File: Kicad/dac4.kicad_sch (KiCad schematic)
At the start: 10 parts

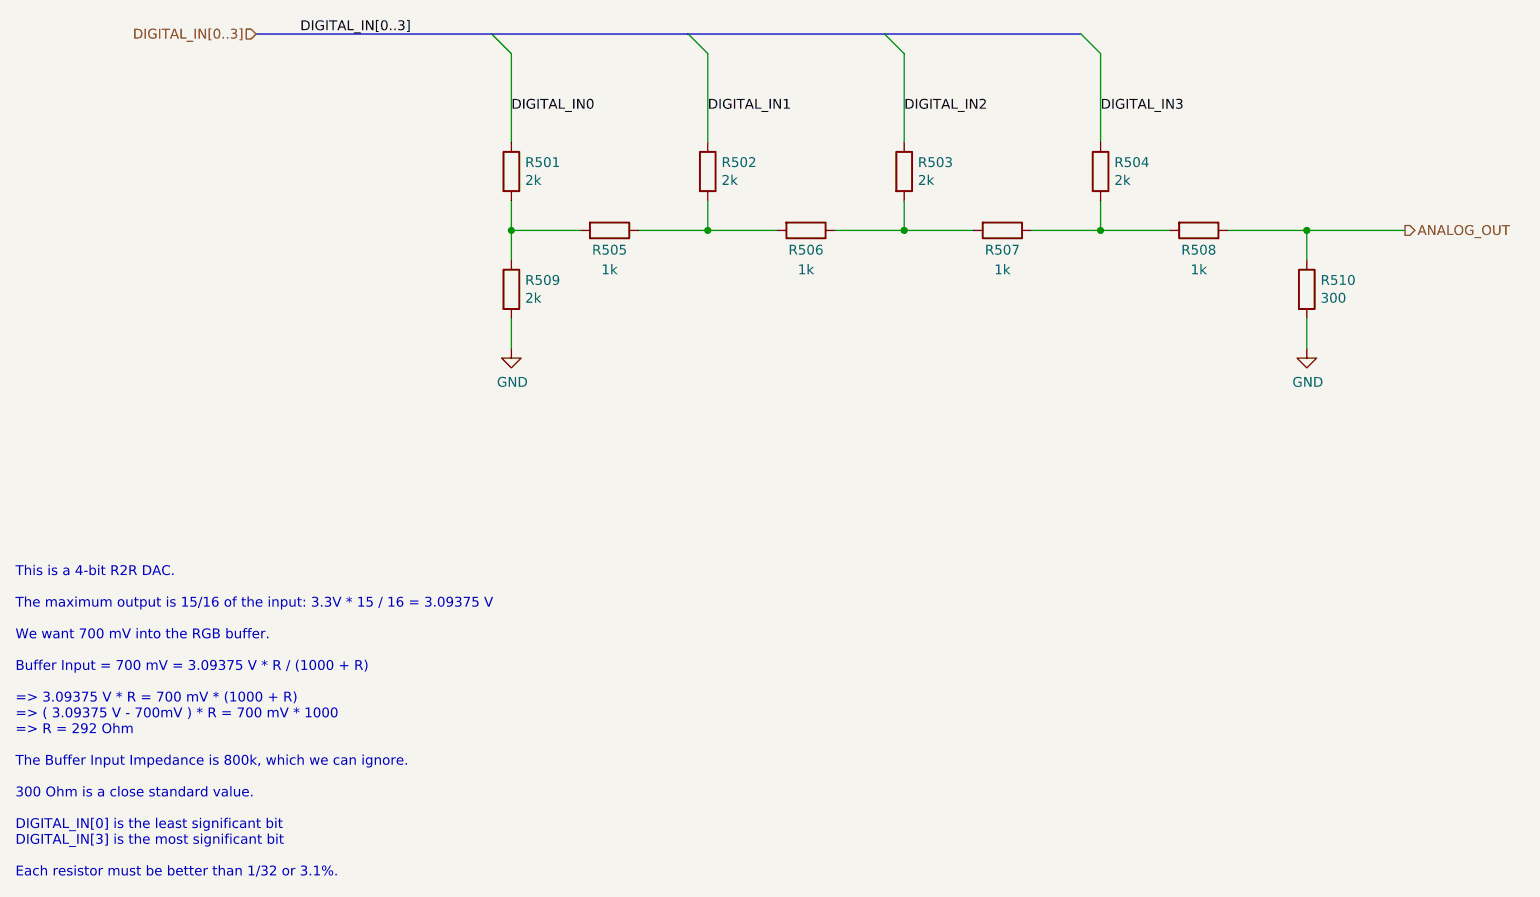
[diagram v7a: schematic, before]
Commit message: Replaced DAC component to fix #177
560R is the best JLCPCB have.
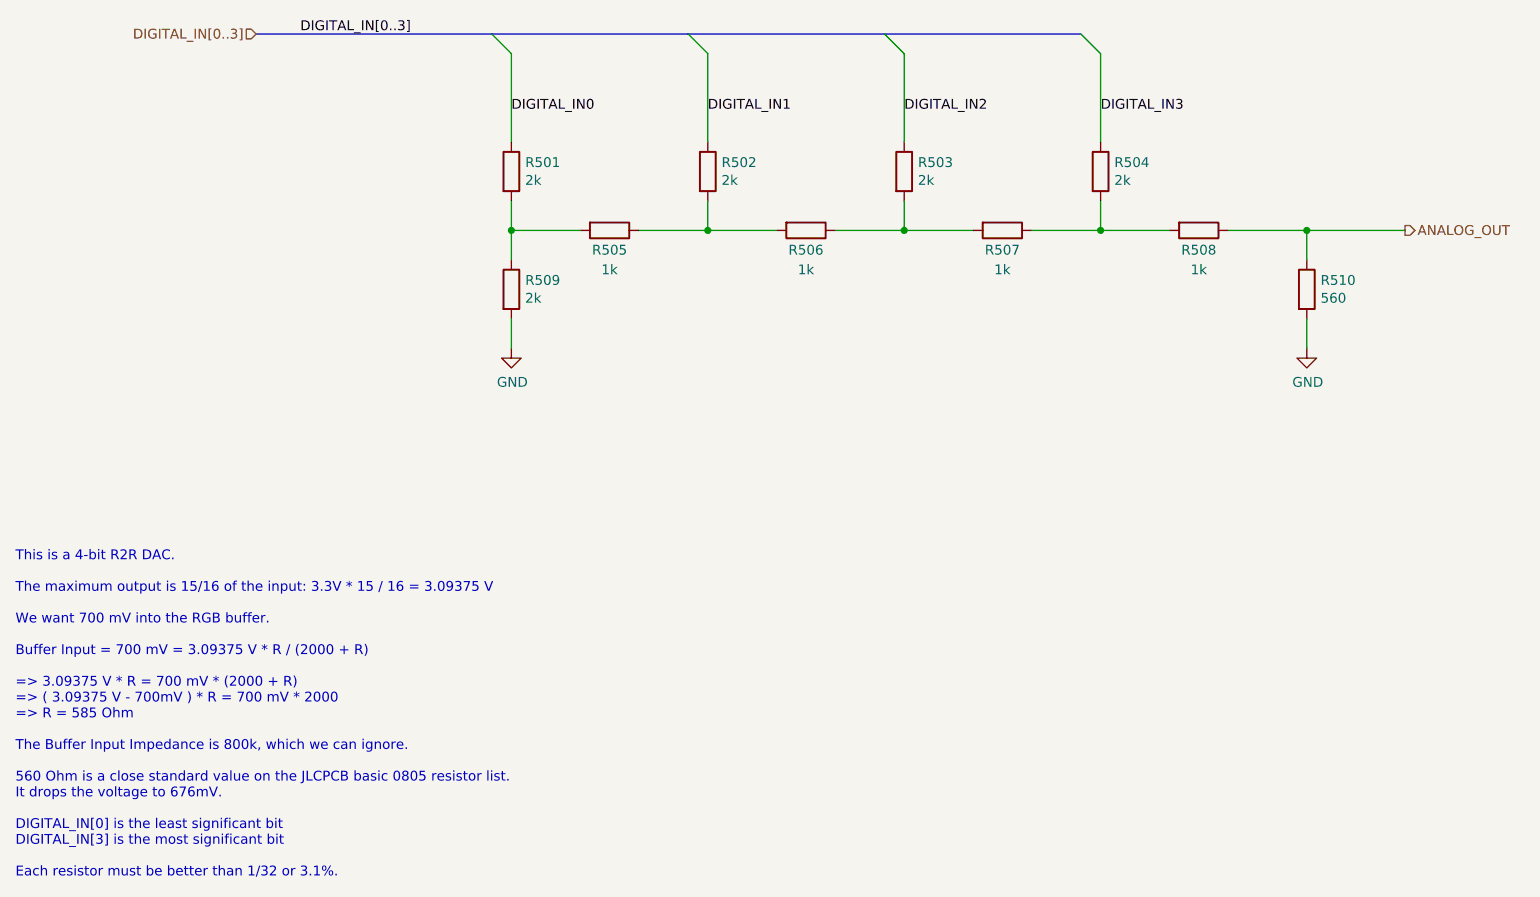
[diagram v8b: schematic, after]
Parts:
- R510: value 300 -> 560; LCSC Part# C17617 -> C28636; MPN 0805W8F3000T5E -> 0805W8F5600T5E
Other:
- note added: "This is a 4-bit R2R DAC. The maximum output is 15/16 of the input: 3.3V * 15 / 16 = 3.09375 V We want 700 mV into the RGB buffer. Buffer Input = 700 mV = 3.09375 V * R / (2000 + R) => 3.09375 V * R = 700 mV * (2000 + R) => ( 3.09375 V - 700mV ) * R = 700 mV * 2000 => R = 585 Ohm The Buffer Input Impedance is 800k, which we can ignore. 560 Ohm is a close standard value on the JLCPCB basic 0805 res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"
- note removed: "This is a 4-bit R2R DAC. The maximum output is 15/16 of the input: 3.3V * 15 / 16 = 3.09375 V We want 700 mV into the RGB buffer. Buffer Input = 700 mV = 3.09375 V * R / (1000 + R) => 3.09375 V * R = 700 mV * (1000 + R) => ( 3.09375 V - 700mV ) * R = 700 mV * 1000 => R = 292 Ohm The Buffer Input Impedance is 800k, which we can ignore. 300 Ohm is a close standard value. DIGITAL_IN[0] is the least 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"
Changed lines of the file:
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@@
     (stroke (width 0) (type default))
   )
-  (text "This is a 4-bit R2R DAC.\n\nThe maximum output is 15/16 of the input: 3.3V * 15 / 16 = 3.09375 V\n\nWe want 700 mV into the RGB buffer.\n\nBuffer Input = 700 mV = 3.09375 V * R / (1000 + R)\n\n=> 3.09375 V * R = 700 mV * (1000 + R)\n=> ( 3.09375 V - 700mV ) * R = 700 mV * 1000\n=> R = 292 Ohm\n\nThe Buffer Input Impedance is 800k, which we can ignore.\n\n300 Ohm is a close standard value.\n\nDIGITAL_IN[0] is the least significant bit\nDIGITAL_IN[3] is the most significant bit\n\nEach resistor must be better than 1/32 or 3.1%.\n"
+  (text "This is a 4-bit R2R DAC.\n\nThe maximum output is 15/16 of the input: 3.3V * 15 / 16 = 3.09375 V\n\nWe want 700 mV into the RGB buffer.\n\nBuffer Input = 700 mV = 3.09375 V * R / (2000 + R)\n\n=> 3.09375 V * R = 700 mV * (2000 + R)\n=> ( 3.09375 V - 700mV ) * R = 700 mV * 2000\n=> R = 585 Ohm\n\nThe Buffer Input Impedance is 800k, which we can ignore.\n\n560 Ohm is a close standard value on the JLCPCB basic 0805 resistor list.\nIt drops the voltage to 676mV.\n\nDIGITAL_IN[0] is the least significant bit\nDIGITAL_IN[3] is the most significant bit\n\nEach resistor must be better than 1/32 or 3.1%.\n"
     (at 24.765 160.02 0)
     (effects (font (size 1.27 1.27)) (justify left bottom))
@@
       (effects (font (size 1.27 1.27)) (justify left))
     )
-    (property "Value" "300" (at 193.548 84.963 0)
+    (property "Value" "560" (at 193.548 84.963 0)
       (effects (font (size 1.27 1.27)) (justify left))
     )
@@
       (effects (font (size 1.27 1.27)) hide)
     )
-    (property "MPN" "0805W8F3000T5E" (at 191.77 83.82 0)
+    (property "MPN" "0805W8F5600T5E" (at 191.77 83.82 0)
       (effects (font (size 1.27 1.27)) hide)
     )
@@
       (effects (font (size 1.27 1.27)) hide)
     )
-    (property "LCSC Part#" "C17617" (at 191.77 83.82 0)
-      (effects (font (size 1.27 1.27)) hide)
-    )
+    (property "LCSC Part#" "C28636" (at 191.77 83.82 0)
+      (effects (font (size 1.27 1.27)) hide)
+    )
